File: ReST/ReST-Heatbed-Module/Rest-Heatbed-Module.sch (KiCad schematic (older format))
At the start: 16 parts, among them P1 02-SCREW-TERM, P2 02X04-MALE, P3 02-SCREW-TERM, P4 01X02-MALE, P5 02-SCREW-TERM, Q1 Q_BSH105, Q2 Q_AOT240L

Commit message: Changes Heatbed + Added Driver Board
Edited Heatbed SMD Footprint from 0805 to 1206, easier to solder for beginners.

Added Schematic and Netlist for Pololu Driver Board
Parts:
- C1: footprint Capacitors_SMD:C_0805_HandSoldering -> ok-smd-generic:1206
- R1, R2, R3, R4, R5: footprint Resistors_SMD:R_0805_HandSoldering -> ok-smd-generic:1206
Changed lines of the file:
@@
 F 0 "R4" V 8680 3550 50  0000 C CNN
 F 1 "22R" V 8600 3550 50  0000 C CNN
-F 2 "Resistors_SMD:R_0805_HandSoldering" V 8530 3550 50  0001 C CNN
+F 2 "ok-smd-generic:1206" V 8530 3550 50  0001 C CNN
 F 3 "" H 8600 3550 50  0000 C CNN
 	1    8600 3550
@@
 F 0 "C1" H 6425 4050 50  0000 L CNN
 F 1 "10uF" H 6425 3850 50  0000 L CNN
-F 2 "Capacitors_SMD:C_0805_HandSoldering" H 6438 3800 50  0001 C CNN
+F 2 "ok-smd-generic:1206" H 6438 3800 50  0001 C CNN
 F 3 "" H 6400 3950 50  0000 C CNN
 	1    6400 3950
@@
 F 0 "R1" V 6480 3550 50  0000 C CNN
 F 1 "4.7K" V 6400 3550 50  0000 C CNN
-F 2 "Resistors_SMD:R_0805_HandSoldering" V 6330 3550 50  0001 C CNN
+F 2 "ok-smd-generic:1206" V 6330 3550 50  0001 C CNN
 F 3 "" H 6400 3550 50  0000 C CNN
 	1    6400 3550
@@
 F 0 "R2" V 8030 3600 50  0000 C CNN
 F 1 "100K" V 7950 3600 50  0000 C CNN
-F 2 "Resistors_SMD:R_0805_HandSoldering" V 7880 3600 50  0001 C CNN
+F 2 "ok-smd-generic:1206" V 7880 3600 50  0001 C CNN
 F 3 "" H 7950 3600 50  0000 C CNN
 	1    7950 3600
@@
 F 0 "R3" V 8430 3300 50  0000 C CNN
 F 1 "100K" V 8350 3300 50  0000 C CNN
-F 2 "Resistors_SMD:R_0805_HandSoldering" V 8280 3300 50  0001 C CNN
+F 2 "ok-smd-generic:1206" V 8280 3300 50  0001 C CNN
 F 3 "" H 8350 3300 50  0000 C CNN
 	1    8350 3300
@@
 F 0 "R5" V 8830 2950 50  0000 C CNN
 F 1 "470R" V 8750 2950 50  0000 C CNN
-F 2 "Resistors_SMD:R_0805_HandSoldering" V 8680 2950 50  0001 C CNN
+F 2 "ok-smd-generic:1206" V 8680 2950 50  0001 C CNN
 F 3 "" H 8750 2950 50  0000 C CNN
 	1    8750 2950

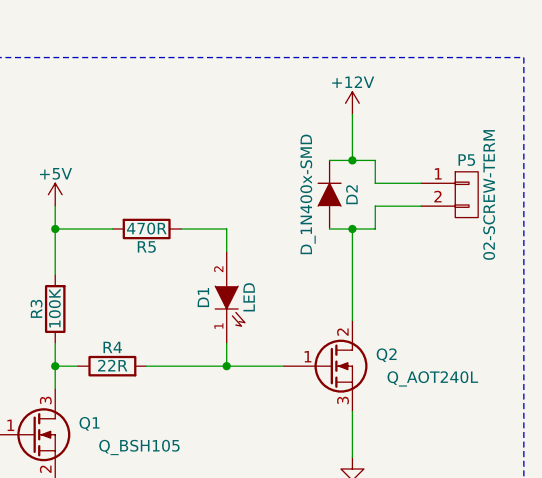
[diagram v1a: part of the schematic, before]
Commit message: Layout for Heatbed PCB
Basic layout for the heatbed pcb is finished. single sided load, so its easier for reflow. need to work on the traces now. size shouldnt change by now.
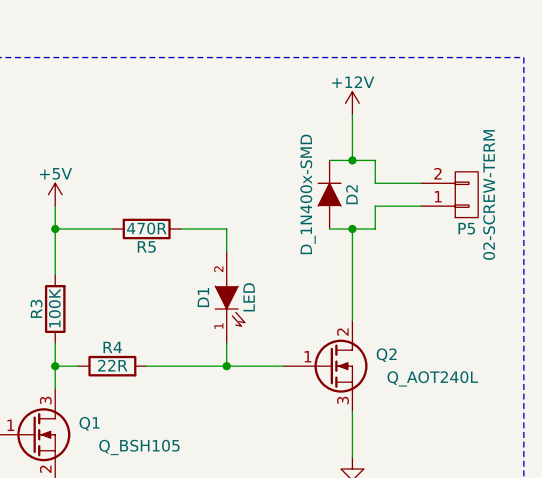
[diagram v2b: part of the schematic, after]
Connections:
- net +12V: now also P5.2 (P2); no longer P5.1 (P1)
- net at D2.2 (A), Q2.2 (D): now also P5.1 (P1); no longer P5.2 (P2)
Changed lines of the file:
@@
 F 3 "" H 10150 2800 50  0000 C CNN
 	1    10150 2800
-	1    0    0    -1
+	1    0    0    1
 $EndComp
 $Comp
@@
 	9950 2750 9750 2750
 Wire Wire Line
-	9750 2750 9750 2650
-Wire Wire Line
-	9750 2650 9550 2650
+	9750 2650 9750 2750
+Wire Wire Line
+	9550 2650 9750 2650
 Wire Wire Line
 	9950 2850 9750 2850
 Wire Wire Line
-	9750 2850 9750 2950
-Wire Wire Line
-	9750 2950 9550 2950
+	9750 2950 9750 2850
+Wire Wire Line
+	9550 2950 9750 2950
 Wire Wire Line
 	9650 2450 9650 2650
